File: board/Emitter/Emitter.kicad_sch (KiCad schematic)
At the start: 15 parts, among them J1 Conn_01x02, Q1 2N3904, Q2 2N7000

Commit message: Adjust values
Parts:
- D1, D2, D3, D4, D5, D6, D7, D8: value LED -> OP294
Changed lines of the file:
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@@
       (effects (font (size 1.27 1.27)) (justify right))
     )
-    (property "Value" "LED" (id 1) (at 135.89 46.1009 90)
+    (property "Value" "OP294" (id 1) (at 135.89 46.1009 90)
       (effects (font (size 1.27 1.27)) (justify right))
     )
@@
       (effects (font (size 1.27 1.27)) (justify right))
     )
-    (property "Value" "LED" (id 1) (at 135.89 53.7209 90)
+    (property "Value" "OP294" (id 1) (at 135.89 53.7209 90)
       (effects (font (size 1.27 1.27)) (justify right))
     )
@@
       (effects (font (size 1.27 1.27)) (justify right))
     )
-    (property "Value" "LED" (id 1) (at 135.89 61.3409 90)
+    (property "Value" "OP294" (id 1) (at 135.89 61.3409 90)
       (effects (font (size 1.27 1.27)) (justify right))
     )
@@
       (effects (font (size 1.27 1.27)) (justify right))
     )
-    (property "Value" "LED" (id 1) (at 135.89 68.9609 90)
+    (property "Value" "OP294" (id 1) (at 135.89 68.9609 90)
       (effects (font (size 1.27 1.27)) (justify right))
     )
@@
       (effects (font (size 1.27 1.27)) (justify right))
     )
-    (property "Value" "LED" (id 1) (at 135.89 76.5809 90)
+    (property "Value" "OP294" (id 1) (at 135.89 76.5809 90)
       (effects (font (size 1.27 1.27)) (justify right))
     )
@@
       (effects (font (size 1.27 1.27)) (justify right))
     )
-    (property "Value" "LED" (id 1) (at 135.89 84.2009 90)
+    (property "Value" "OP294" (id 1) (at 135.89 84.2009 90)
       (effects (font (size 1.27 1.27)) (justify right))
     )
@@
       (effects (font (size 1.27 1.27)) (justify right))
     )
-    (property "Value" "LED" (id 1) (at 135.89 91.8209 90)
+    (property "Value" "OP294" (id 1) (at 135.89 91.8209 90)
       (effects (font (size 1.27 1.27)) (justify right))
     )
@@
       (effects (font (size 1.27 1.27)) (justify right))
     )
-    (property "Value" "LED" (id 1) (at 135.89 99.4409 90)
+    (property "Value" "OP294" (id 1) (at 135.89 99.4409 90)
       (effects (font (size 1.27 1.27)) (justify right))
     )
@@
     )
     (path "/fc5686c0-c9a0-4b43-aba4-db38c23df62c"
-      (reference "D1") (unit 1) (value "LED") (footprint "LED_THT:LED_D5.0mm_IRGrey")
+      (reference "D1") (unit 1) (value "OP294") (footprint "LED_THT:LED_D5.0mm_IRGrey")
     )
     (path "/0f84b10e-7b49-4869-a692-afaba5aac0fa"
-      (reference "D2") (unit 1) (value "LED") (footprint "LED_THT:LED_D5.0mm_IRGrey")
+      (reference "D2") (unit 1) (value "OP294") (footprint "LED_THT:LED_D5.0mm_IRGrey")
     )
     (path "/3719e729-1573-4065-bc20-bbd92e0eb185"
-      (reference "D3") (unit 1) (value "LED") (footprint "LED_THT:LED_D5.0mm_IRGrey")
+      (reference "D3") (unit 1) (value "OP294") (footprint "LED_THT:LED_D5.0mm_IRGrey")
     )
     (path "/92e5fdf2-972b-455e-a46b-013ec7b9fe23"
-      (reference "D4") (unit 1) (value "LED") (footprint "LED_THT:LED_D5.0mm_IRGrey")
+      (reference "D4") (unit 1) (value "OP294") (footprint "LED_THT:LED_D5.0mm_IRGrey")
     )
     (path "/6bf576f9-61ef-4262-bf9b-d3d9d19f3b88"
-      (reference "D5") (unit 1) (value "LED") (footprint "LED_THT:LED_D5.0mm_IRGrey")
+      (reference "D5") (unit 1) (value "OP294") (footprint "LED_THT:LED_D5.0mm_IRGrey")
     )
     (path "/e7fa291e-b593-4182-be4d-0029a5f16e81"
-      (reference "D6") (unit 1) (value "LED") (footprint "LED_THT:LED_D5.0mm_IRGrey")
+      (reference "D6") (unit 1) (value "OP294") (footprint "LED_THT:LED_D5.0mm_IRGrey")
     )
     (path "/7f0e7b67-475d-4dc7-b67d-23ce0c9528c5"
-      (reference "D7") (unit 1) (value "LED") (footprint "LED_THT:LED_D5.0mm_IRGrey")
+      (reference "D7") (unit 1) (value "OP294") (footprint "LED_THT:LED_D5.0mm_IRGrey")
     )
     (path "/16b28e35-6aaa-43ec-8c2b-3c54ee684ec7"
-      (reference "D8") (unit 1) (value "LED") (footprint "LED_THT:LED_D5.0mm_IRGrey")
+      (reference "D8") (unit 1) (value "OP294") (footprint "LED_THT:LED_D5.0mm_IRGrey")
     )
     (path "/db6f75d8-364c-44f9-8201-fa5395e4696a"

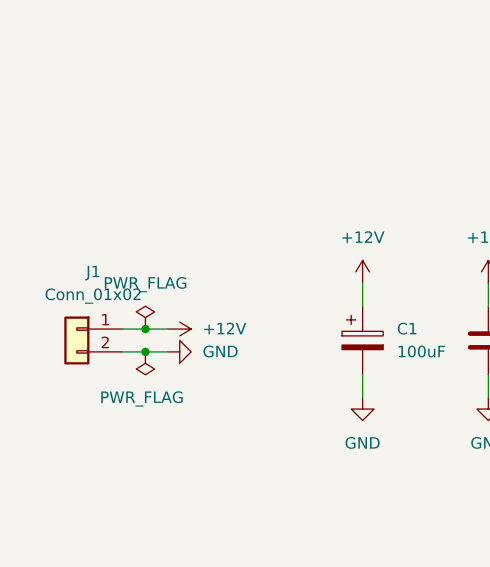
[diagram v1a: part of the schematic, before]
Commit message: Changed connectors, 3D models, added test points
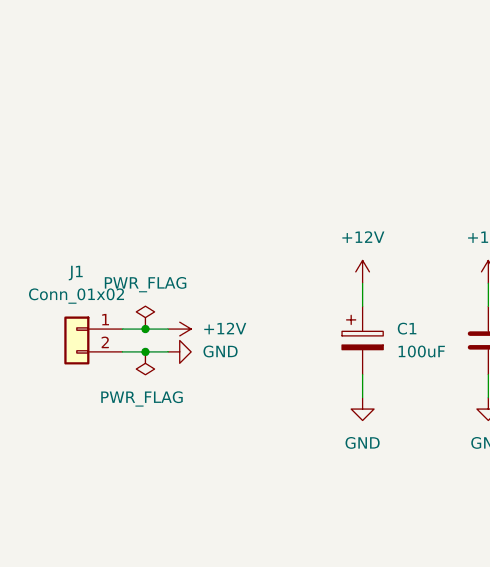
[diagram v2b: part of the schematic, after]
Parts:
- J1: footprint SaintGimp:KF2510_Header_1x02_Vertical -> TerminalBlock_TE-Connectivity:TerminalBlock_TE_282834-2_1x02_P2.54mm_Horizontal
